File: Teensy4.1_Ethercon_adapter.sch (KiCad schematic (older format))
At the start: 10 parts, among them J1 Conn_01x06, J2 NE8FAV

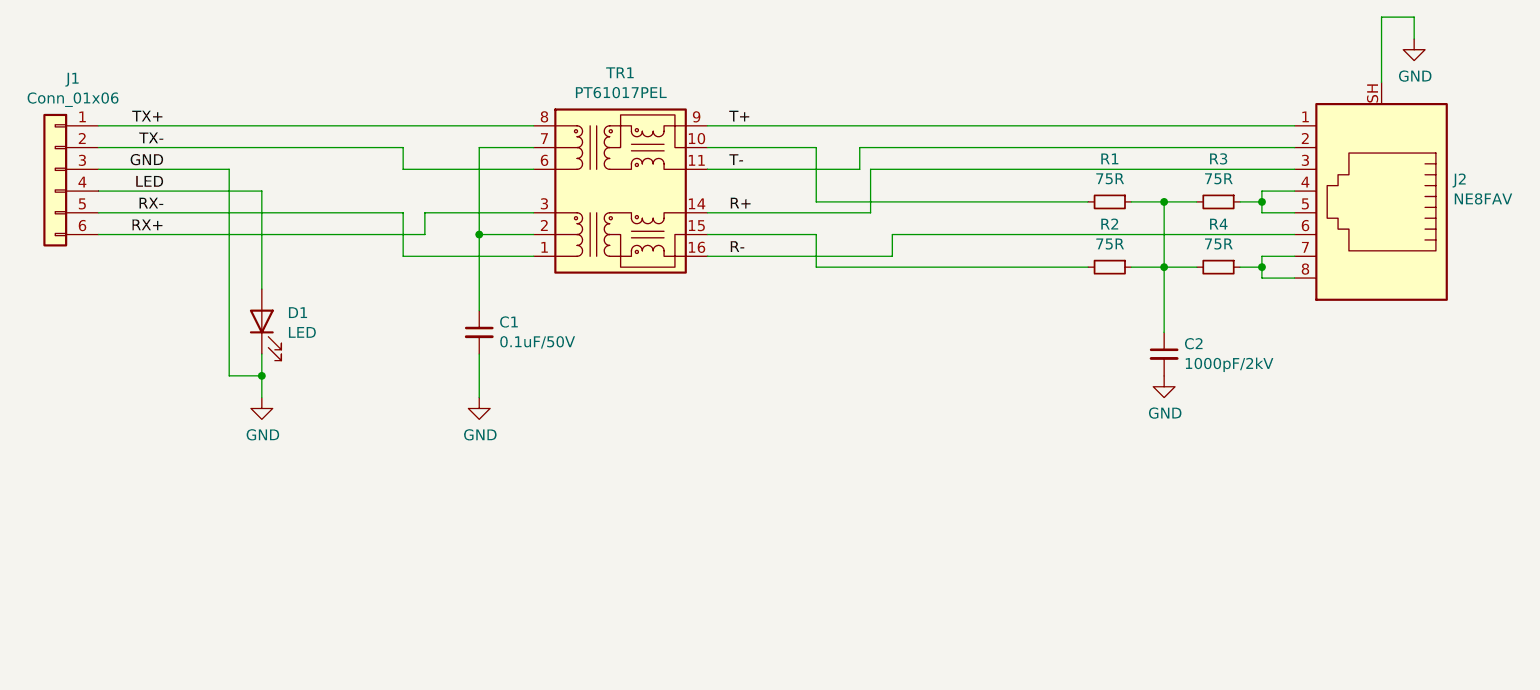
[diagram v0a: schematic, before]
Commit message: Version 1.1 - fixed routing and pin header pitch (2mm)
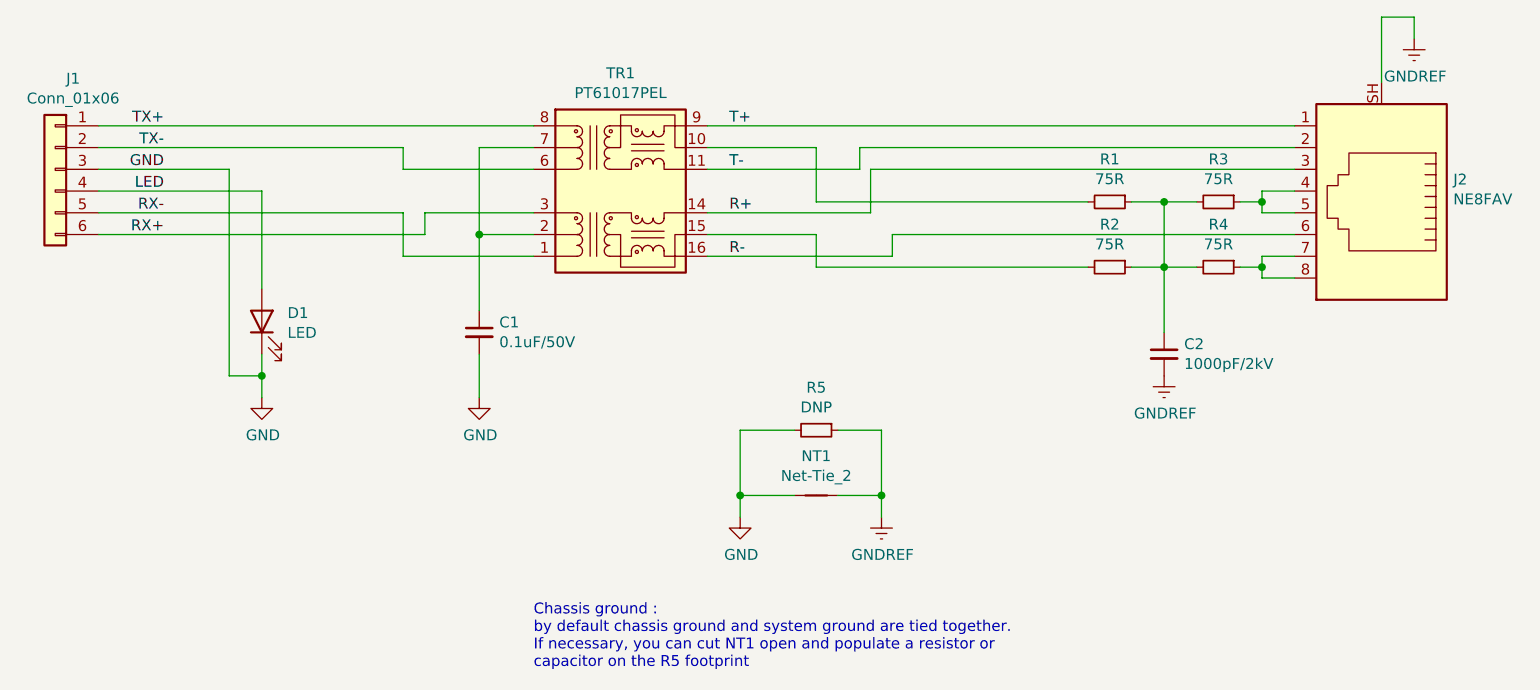
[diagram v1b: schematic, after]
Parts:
- added NT1: Net-Tie_2, NetTie:NetTie-2_SMD_Pad0.5mm, symbol Device:Net-Tie_2
- added R5: DNP, Resistor_SMD:R_0805_2012Metric, symbol Device:R_Small
- J1: footprint Connector_PinHeader_2.54mm:PinHeader_2x03_P2.54mm_Vertical -> Connector_PinHeader_2.00mm:PinHeader_2x03_P2.00mm_Vertical
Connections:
- net GND: now also NT1.1, R5.2; no longer C2.2, J2.SH
- new net GNDREF: C2.2, J2.SH, NT1.2, R5.1
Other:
- note added: "Chassis ground :\nby default chassis ground and system ground are tied together.\nIf necessary, you can cut NT1 open and populate a resistor or \ncapacitor on the R5 footprint"
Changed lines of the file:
@@
 Sheet 1 1
 Title "Teensy 4.1 Ethercon adapter"
-Date "2021-01-28"
-Rev "1.0"
+Date "2021-03-17"
+Rev "1.1"
 Comp "Tom Magnier"
 Comment1 ""
@@
 F 0 "J1" H 3618 3517 50  0000 C CNN
 F 1 "Conn_01x06" H 3618 3426 50  0000 C CNN
-F 2 "Connector_PinHeader_2.54mm:PinHeader_2x03_P2.54mm_Vertical" H 3700 3100 50  0001 C CNN
+F 2 "Connector_PinHeader_2.00mm:PinHeader_2x03_P2.00mm_Vertical" H 3700 3100 50  0001 C CNN
 F 3 "~" H 3700 3100 50  0001 C CNN
 	1    3700 3100
@@
 Wire Wire Line
 	8800 3550 8800 3850
-$Comp
-L power:GND #PWR0103
-U 1 1 6051E6E5
-P 9950 2500
-F 0 "#PWR0103" H 9950 2250 50  0001 C CNN
-F 1 "GND" H 9955 2327 50  0000 C CNN
-F 2 "" H 9950 2500 50  0001 C CNN
-F 3 "" H 9950 2500 50  0001 C CNN
-	1    9950 2500
-	1    0    0    -1
-$EndComp
 Wire Wire Line
 	9950 2500 9950 2400
@@
 Wire Wire Line
 	9800 2400 9800 2700
-$Comp
-L power:GND #PWR0104
-U 1 1 6051FE15
-P 8800 4050
-F 0 "#PWR0104" H 8800 3800 50  0001 C CNN
-F 1 "GND" H 8805 3877 50  0000 C CNN
-F 2 "" H 8800 4050 50  0001 C CNN
-F 3 "" H 8800 4050 50  0001 C CNN
-	1    8800 4050
-	1    0    0    -1
-$EndComp
 Text Label 6800 2900 0    50   ~ 0
 T+
@@
 	1    0    0    -1
 $EndComp
+$Comp
+L power:GNDREF #PWR03
+U 1 1 60523364
+P 8800 4050
+F 0 "#PWR03" H 8800 3800 50  0001 C CNN
+F 1 "GNDREF" H 8805 3877 50  0000 C CNN
+F 2 "" H 8800 4050 50  0001 C CNN
+F 3 "" H 8800 4050 50  0001 C CNN
+	1    8800 4050
+	1    0    0    -1
+$EndComp
+$Comp
+L power:GNDREF #PWR04
+U 1 1 60526B84
+P 9950 2500
+F 0 "#PWR04" H 9950 2250 50  0001 C CNN
+F 1 "GNDREF" H 9955 2327 50  0000 C CNN
+F 2 "" H 9950 2500 50  0001 C CNN
+F 3 "" H 9950 2500 50  0001 C CNN
+	1    9950 2500
+	1    0    0    -1
+$EndComp
+$Comp
+L Device:R_Small R5
+U 1 1 6052AE76
+P 7200 4300
+F 0 "R5" V 7004 4300 50  0000 C CNN
+F 1 "DNP" V 7095 4300 50  0000 C CNN
+F 2 "Resistor_SMD:R_0805_2012Metric" H 7200 4300 50  0001 C CNN
+F 3 "~" H 7200 4300 50  0001 C CNN
+	1    7200 4300
+	0    1    1    0
+$EndComp
+$Comp
+L Device:Net-Tie_2 NT1
+U 1 1 6052BD96
+P 7200 4600
+F 0 "NT1" H 7200 4781 50  0000 C CNN
+F 1 "Net-Tie_2" H 7200 4690 50  0000 C CNN
+F 2 "NetTie:NetTie-2_SMD_Pad0.5mm" H 7200 4600 50  0001 C CNN
+F 3 "~" H 7200 4600 50  0001 C CNN
+	1    7200 4600
+	1    0    0    -1
+$EndComp
+$Comp
+L power:GNDREF #PWR02
+U 1 1 6052C72B
+P 7500 4700
+F 0 "#PWR02" H 7500 4450 50  0001 C CNN
+F 1 "GNDREF" H 7505 4527 50  0000 C CNN
+F 2 "" H 7500 4700 50  0001 C CNN
+F 3 "" H 7500 4700 50  0001 C CNN
+	1    7500 4700
+	1    0    0    -1
+$EndComp
+Wire Wire Line
+	7500 4700 7500 4600
+Wire Wire Line
+	7500 4600 7300 4600
+Wire Wire Line
+	7500 4600 7500 4300
+Wire Wire Line
+	7500 4300 7300 4300
+Connection ~ 7500 4600
+$Comp
+L power:GND #PWR01
+U 1 1 6052F266
+P 6850 4700
+F 0 "#PWR01" H 6850 4450 50  0001 C CNN
+F 1 "GND" H 6855 4527 50  0000 C CNN
+F 2 "" H 6850 4700 50  0001 C CNN
+F 3 "" H 6850 4700 50  0001 C CNN
+	1    6850 4700
+	1    0    0    -1
+$EndComp
+Wire Wire Line
+	6850 4700 6850 4600
+Wire Wire Line
+	6850 4600 7100 4600
+Wire Wire Line
+	6850 4600 6850 4300
+Wire Wire Line
+	6850 4300 7100 4300
+Connection ~ 6850 4600
+Text Notes 5900 5400 0    50   ~ 0
+Chassis ground :\nby default chassis ground and system ground are tied together.\nIf necessary, you can cut NT1 open and populate a resistor or \ncapacitor on the R5 footprint
 $EndSCHEMATC
